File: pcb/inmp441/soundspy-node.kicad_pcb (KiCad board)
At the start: 2 copper layers, 30 x 68 mm, 9 parts, among them U1_L ESP32_L, U1_R ESP32_R

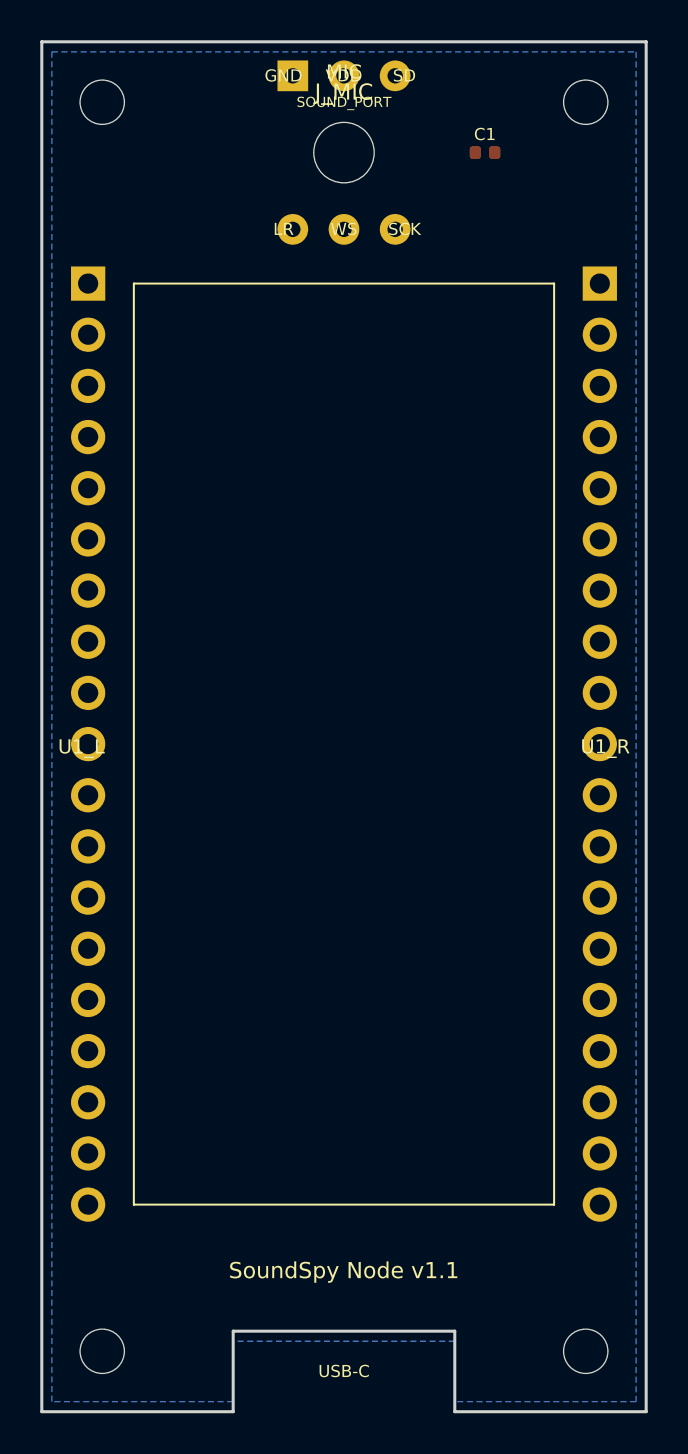
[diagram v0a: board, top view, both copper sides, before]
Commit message: PCB v1.2: routed traces, correct 2x3 mic footprint, no crossings
- 3V3/GND/SCK/WS on F.Cu, SD on B.Cu via vias (no crossings)
- Correct INMP441 footprint: 2x3, drill 0.762mm, pad 1.524mm
- Sound port hole 3mm, J_MIC at y=10 for board clearance
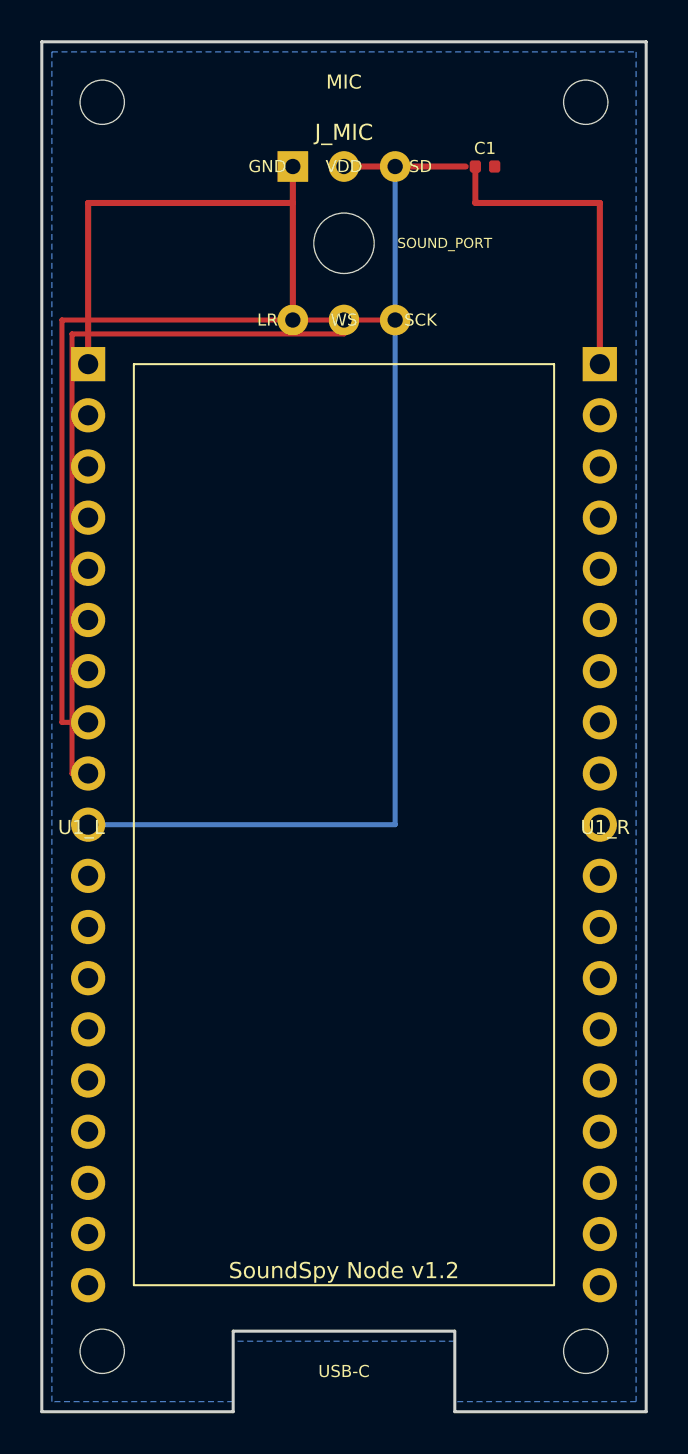
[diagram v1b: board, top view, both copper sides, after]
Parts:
- J_MIC: value INMP441-Breakout -> INMP441
- moved J_MIC 4.50 mm to (15.0, 10.0)
- moved SOUND_PORT 4.50 mm to (15.0, 10.0)
- moved U1_L 4.00 mm to (2.30, 16.0)
- moved U1_R 4.00 mm to (27.7, 16.0)
- moved C1 0.69 mm to (22.0, 6.19)
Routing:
- net I2S_SD: track 0.00 -> 47.9 mm, vias 0 -> 2
- net I2S_SCK: track 0.00 -> 37.8 mm
- net I2S_WS: track 0.00 -> 36.8 mm
- net GND: track 0.00 -> 25.8 mm
- net 3V3: track 0.00 -> 22.0 mm
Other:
- board text added: "SoundSpy Node v1.2"
- board text removed: "SoundSpy Node v1.1"
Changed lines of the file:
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@@
   (title_block
     (title "SoundSpy Node Carrier")
-    (date "2026-07-30")
-    (rev "1.1")
-    (comment 1 "ESP32 38-pin DevKit + INMP441/ICS-43434 circular breakout carrier")
+    (date "2026-07-31")
+    (rev "1.2")
+    (comment 1 "ESP32 38-pin DevKit + INMP441 circular mic module carrier")
     (comment 2 "USB-C notch at bottom for case passthrough")
-    (comment 3 "Mic module: 14mm dia, 2x3 header 2.54mm col / 7.62mm row pitch")
+    (comment 3 "Mic: 14mm dia, 2x3 header, 2.54mm col / 7.62mm row pitch")
   )
   (layers
@@
     (pad "" np_thru_hole circle (at 0 0) (size 2.2 2.2) (drill 2.2) (layers "*.Cu" "*.Mask") (uuid "mhp000004"))
   )
-  (footprint "Connector_PinHeader_2.54mm:PinHeader_2x03_P2.54mm_Vertical" (at 15 5.5 0) (layer "F.Cu")
-    (fp_text reference "J_MIC" (at 0 -3.0) (layer "F.SilkS") (effects (font (size 0.8 0.8) (thickness 0.12))))
-    (fp_text value "INMP441-Breakout" (at 0 3.5) (layer "F.Fab") (effects (font (size 0.7 0.7) (thickness 0.1))))
-    (fp_text user "GND" (at -3.0 -3.81 0) (layer "F.SilkS") (effects (font (size 0.6 0.6) (thickness 0.09))))
-    (fp_text user "VDD" (at 0 -3.81 0)    (layer "F.SilkS") (effects (font (size 0.6 0.6) (thickness 0.09))))
-    (fp_text user "SD"  (at 3.0 -3.81 0)  (layer "F.SilkS") (effects (font (size 0.6 0.6) (thickness 0.09))))
-    (fp_text user "LR"  (at -3.0 3.81 0)  (layer "F.SilkS") (effects (font (size 0.6 0.6) (thickness 0.09))))
-    (fp_text user "WS"  (at 0 3.81 0)     (layer "F.SilkS") (effects (font (size 0.6 0.6) (thickness 0.09))))
-    (fp_text user "SCK" (at 3.0 3.81 0)   (layer "F.SilkS") (effects (font (size 0.6 0.6) (thickness 0.09))))
+  (footprint "Connector_PinHeader_2.54mm:PinHeader_2x03_P2.54mm_Vertical" (at 15 10.0 0) (layer "F.Cu")
+    (fp_text reference "J_MIC" (at 0 -5.5) (layer "F.SilkS") (effects (font (size 0.8 0.8) (thickness 0.12))))
+    (fp_text value "INMP441" (at 0 5.5) (layer "F.Fab") (effects (font (size 0.7 0.7) (thickness 0.1))))
+    (fp_text user "GND" (at -3.8 -3.81 0) (layer "F.SilkS") (effects (font (size 0.6 0.6) (thickness 0.09))))
+    (fp_text user "VDD" (at 0    -3.81 0) (layer "F.SilkS") (effects (font (size 0.6 0.6) (thickness 0.09))))
+    (fp_text user "SD"  (at 3.8  -3.81 0) (layer "F.SilkS") (effects (font (size 0.6 0.6) (thickness 0.09))))
+    (fp_text user "LR"  (at -3.8  3.81 0) (layer "F.SilkS") (effects (font (size 0.6 0.6) (thickness 0.09))))
+    (fp_text user "WS"  (at 0     3.81 0) (layer "F.SilkS") (effects (font (size 0.6 0.6) (thickness 0.09))))
+    (fp_text user "SCK" (at 3.8   3.81 0) (layer "F.SilkS") (effects (font (size 0.6 0.6) (thickness 0.09))))
     (pad "1" thru_hole rect   (at -2.54 -3.81) (size 1.524 1.524) (drill 0.762) (layers "*.Cu" "*.Mask") (net 2 "GND"))
-    (pad "2" thru_hole circle (at 0     -3.81) (size 1.524 1.524) (drill 0.762) (layers "*.Cu" "*.Mask") (net 1 "3V3"))
-    (pad "3" thru_hole circle (at 2.54  -3.81) (size 1.524 1.524) (drill 0.762) (layers "*.Cu" "*.Mask") (net 4 "I2S_SD"))
+    (pad "2" thru_hole circle (at  0.00 -3.81) (size 1.524 1.524) (drill 0.762) (layers "*.Cu" "*.Mask") (net 1 "3V3"))
+    (pad "3" thru_hole circle (at  2.54 -3.81) (size 1.524 1.524) (drill 0.762) (layers "*.Cu" "*.Mask") (net 4 "I2S_SD"))
     (pad "4" thru_hole circle (at -2.54  3.81) (size 1.524 1.524) (drill 0.762) (layers "*.Cu" "*.Mask") (net 6 "I2S_LR"))
-    (pad "5" thru_hole circle (at 0      3.81) (size 1.524 1.524) (drill 0.762) (layers "*.Cu" "*.Mask") (net 3 "I2S_WS"))
-    (pad "6" thru_hole circle (at 2.54   3.81) (size 1.524 1.524) (drill 0.762) (layers "*.Cu" "*.Mask") (net 5 "I2S_SCK"))
+    (pad "5" thru_hole circle (at  0.00  3.81) (size 1.524 1.524) (drill 0.762) (layers "*.Cu" "*.Mask") (net 3 "I2S_WS"))
+    (pad "6" thru_hole circle (at  2.54  3.81) (size 1.524 1.524) (drill 0.762) (layers "*.Cu" "*.Mask") (net 5 "I2S_SCK"))
   )
-  (footprint "MountingHole:MountingHole_3.2mm" (at 15 5.5) (layer "F.Cu")
-    (fp_text reference "SOUND_PORT" (at 0 -2.5) (layer "F.SilkS") (effects (font (size 0.5 0.5) (thickness 0.08))))
+  (footprint "MountingHole:MountingHole_3.2mm" (at 15 10.0) (layer "F.Cu")
+    (fp_text reference "SOUND_PORT" (at 5 0) (layer "F.SilkS") (effects (font (size 0.5 0.5) (thickness 0.08))))
     (pad "" np_thru_hole circle (at 0 0) (size 3.0 3.0) (drill 3.0) (layers "*.Cu" "*.Mask"))
   )
-  (footprint "Capacitor_SMD:C_0402_1005Metric" (at 22 5.5 0) (layer "F.Cu")
+  (footprint "Capacitor_SMD:C_0402_1005Metric" (at 22.0 6.19 0) (layer "F.Cu")
     (fp_text reference "C1" (at 0 -0.9) (layer "F.SilkS") (effects (font (size 0.6 0.6) (thickness 0.1))))
     (fp_text value "100nF" (at 0 0.9) (layer "F.Fab") (effects (font (size 0.6 0.6) (thickness 0.1))))
@@
     (pad "2" smd roundrect (at  0.48 0) (size 0.56 0.62) (layers "F.Cu" "F.Mask" "F.Paste") (roundrect_rratio 0.25) (net 2 "GND"))
   )
-  (footprint "Connector_PinHeader_2.54mm:PinHeader_1x19_P2.54mm_Vertical" (at 2.3 12.0 0) (layer "F.Cu")
+  (footprint "Connector_PinHeader_2.54mm:PinHeader_1x19_P2.54mm_Vertical" (at 2.3 16.0 0) (layer "F.Cu")
     (uuid "esp000001")
     (fp_text reference "U1_L" (at -1.5 23.0) (layer "F.SilkS") (effects (font (size 0.7 0.7) (thickness 0.1)) (justify left)) (uuid "espe000001"))
@@
     (pad "19" thru_hole circle (at 0 45.72)  (size 1.7 1.7) (drill 1.0) (layers "*.Cu" "*.Mask") (net 0 "")        (uuid "espl000019"))
   )
-  (footprint "Connector_PinHeader_2.54mm:PinHeader_1x19_P2.54mm_Vertical" (at 27.7 12.0 0) (layer "F.Cu")
+  (footprint "Connector_PinHeader_2.54mm:PinHeader_1x19_P2.54mm_Vertical" (at 27.7 16.0 0) (layer "F.Cu")
     (uuid "esp000002")
     (fp_text reference "U1_R" (at 1.5 23.0) (layer "F.SilkS") (effects (font (size 0.7 0.7) (thickness 0.1)) (justify right)) (uuid "espe000003"))
@@
     (pad "19" thru_hole circle (at 0 45.72)  (size 1.7 1.7) (drill 1.0) (layers "*.Cu" "*.Mask") (net 0 "")     (uuid "espr000019"))
   )
-  (gr_text "SoundSpy Node v1.1" (at 15 61.0) (layer "F.SilkS")
+  (segment (start 27.7 16.0)   (end 27.7 8.0)    (width 0.3)  (layer "F.Cu") (net 1) (uuid "tr3v3_1"))
+  (segment (start 27.7 8.0)    (end 21.52 8.0)   (width 0.3)  (layer "F.Cu") (net 1) (uuid "tr3v3_2"))
+  (segment (start 21.52 8.0)   (end 21.52 6.19)  (width 0.3)  (layer "F.Cu") (net 1) (uuid "tr3v3_3"))
+  (segment (start 15.0 6.19)   (end 21.04 6.19)  (width 0.3)  (layer "F.Cu") (net 1) (uuid "tr3v3_4"))
+  (segment (start 2.3 16.0)    (end 2.3 8.0)     (width 0.3)  (layer "F.Cu") (net 2) (uuid "trgnd_1"))
+  (segment (start 2.3 8.0)     (end 12.46 8.0)   (width 0.3)  (layer "F.Cu") (net 2) (uuid "trgnd_2"))
+  (segment (start 12.46 8.0)   (end 12.46 6.19)  (width 0.3)  (layer "F.Cu") (net 2) (uuid "trgnd_3"))
+  (segment (start 12.46 13.81) (end 12.46 8.0)   (width 0.3)  (layer "F.Cu") (net 2) (uuid "trgnd_lr"))
+  (segment (start 2.3 33.78)   (end 1.0 33.78)   (width 0.25) (layer "F.Cu") (net 5) (uuid "trsck_1"))
+  (segment (start 1.0 33.78)   (end 1.0 13.81)   (width 0.25) (layer "F.Cu") (net 5) (uuid "trsck_2"))
+  (segment (start 1.0 13.81)   (end 17.54 13.81) (width 0.25) (layer "F.Cu") (net 5) (uuid "trsck_3"))
+  (segment (start 2.3 36.32)   (end 1.5 36.32)   (width 0.25) (layer "F.Cu") (net 3) (uuid "trws_1"))
+  (segment (start 1.5 36.32)   (end 1.5 14.5)    (width 0.25) (layer "F.Cu") (net 3) (uuid "trws_2"))
+  (segment (start 1.5 14.5)    (end 15.0 14.5)   (width 0.25) (layer "F.Cu") (net 3) (uuid "trws_3"))
+  (segment (start 15.0 14.5)   (end 15.0 13.81)  (width 0.25) (layer "F.Cu") (net 3) (uuid "trws_4"))
+  (via (at 2.3 38.86)  (size 0.8) (drill 0.4) (layers "F.Cu" "B.Cu") (net 4) (uuid "via_sd_1"))
+  (via (at 17.54 6.19) (size 0.8) (drill 0.4) (layers "F.Cu" "B.Cu") (net 4) (uuid "via_sd_2"))
+  (segment (start 2.3 38.86)   (end 17.54 38.86) (width 0.25) (layer "B.Cu") (net 4) (uuid "trsd_1"))
+  (segment (start 17.54 38.86) (end 17.54 6.19)  (width 0.25) (layer "B.Cu") (net 4) (uuid "trsd_2"))
+  (gr_text "SoundSpy Node v1.2" (at 15 61.0) (layer "F.SilkS")
     (effects (font (size 0.8 0.8) (thickness 0.12)))
   )
-  (gr_text "MIC" (at 15 1.5) (layer "F.SilkS")
+  (gr_text "MIC" (at 15 2.0) (layer "F.SilkS")
     (effects (font (size 0.7 0.7) (thickness 0.1)))
   )
@@
     (effects (font (size 0.6 0.6) (thickness 0.09)))
   )
-  (gr_rect (start 4.57 12.0) (end 25.43 57.72) (layer "F.SilkS") (width 0.1))
+  (gr_rect (start 4.57 16.0) (end 25.43 61.72) (layer "F.SilkS") (width 0.1))
   (zone (net 2) (net_name "GND") (layer "B.Cu")
     (hatch edge 0.5)

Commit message: Add 3D-printable enclosure; update carrier PCB to printed rev 1.2
- case/: parametric OpenSCAD base + lid for the 30x68 carrier, ESP32 on
  female sockets, lid grille and end-wall slots over the mic, USB-C
  cutout, M2 standoffs and lid columns, keyhole wall mount
- part="fitcheck" intersects the case with board part volumes;
  scripts/render_case.sh fails if anything collides
- pcb: replace with the file sent to fab (mic at 15,9 facing up, no sound
  hole, THT C1, routed) and update DESIGN.md
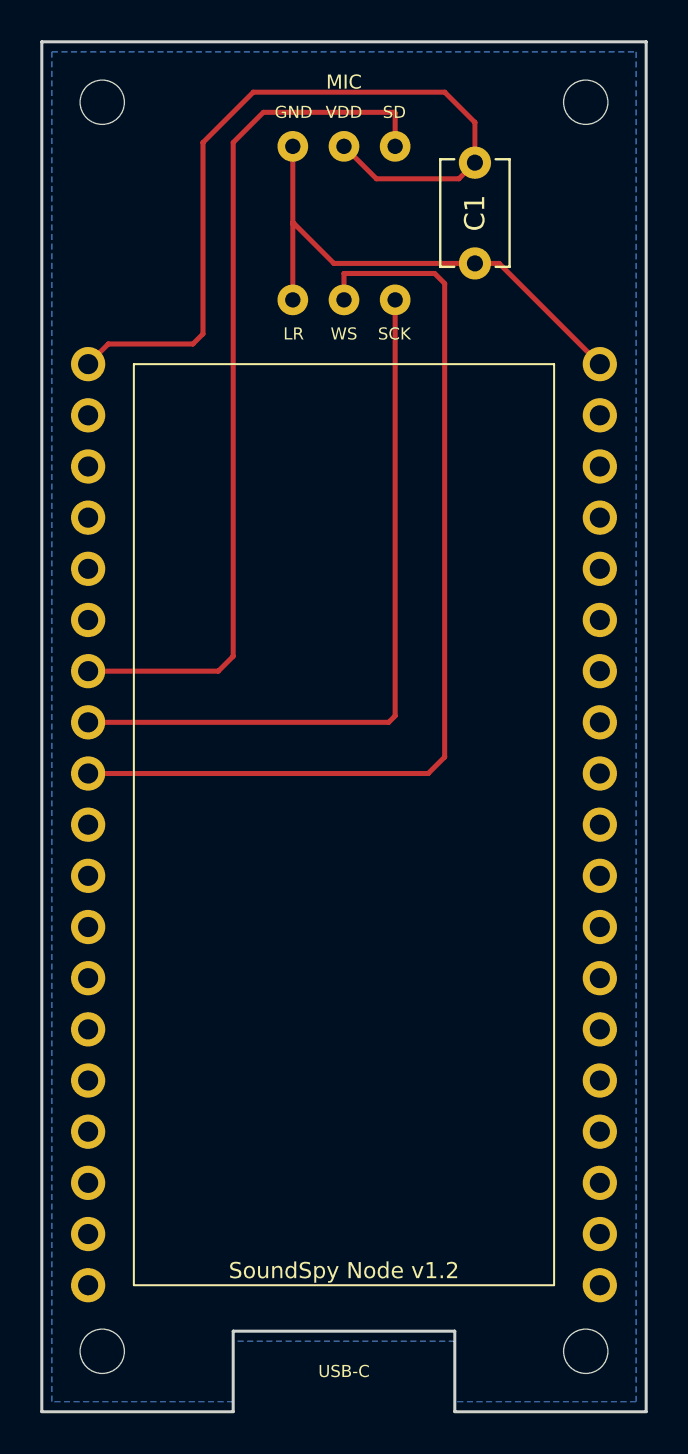
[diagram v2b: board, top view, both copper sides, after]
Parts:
- removed SOUND_PORT: , MountingHole:MountingHole_3.2mm
- C1: value 100nF -> C_Disc_D5.1mm_W3.2mm_P5.00mm; footprint Capacitor_SMD:C_0402_1005Metric -> Capacitor_THT:C_Disc_D5.1mm_W3.2mm_P5.00mm
- moved C1 4.84 mm to (21.5, 11.0), turned to 90 degrees
- moved MIC 1.00 mm to (15.0, 9.00)
- renumbered J_MIC to MIC
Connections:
- C1 pad 1: 3V3 -> GND
- C1 pad 2: GND -> 3V3
- MIC pad 4: I2S_LR -> GND
- U1_L pad 1: GND -> 3V3
- U1_L pad 10: I2S_SD -> (no net)
- U1_L pad 7: (no net) -> I2S_SD
- U1_R pad 1: 3V3 -> GND
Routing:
- net 3V3: track 22.0 -> 40.5 mm
- net I2S_WS: track 36.8 -> 48.1 mm
- net I2S_SD: track 47.9 -> 43.3 mm, vias 2 -> 0
- net I2S_SCK: track 37.8 -> 36.0 mm
